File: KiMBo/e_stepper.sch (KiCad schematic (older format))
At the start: 24 parts, among them U18 TMC2130

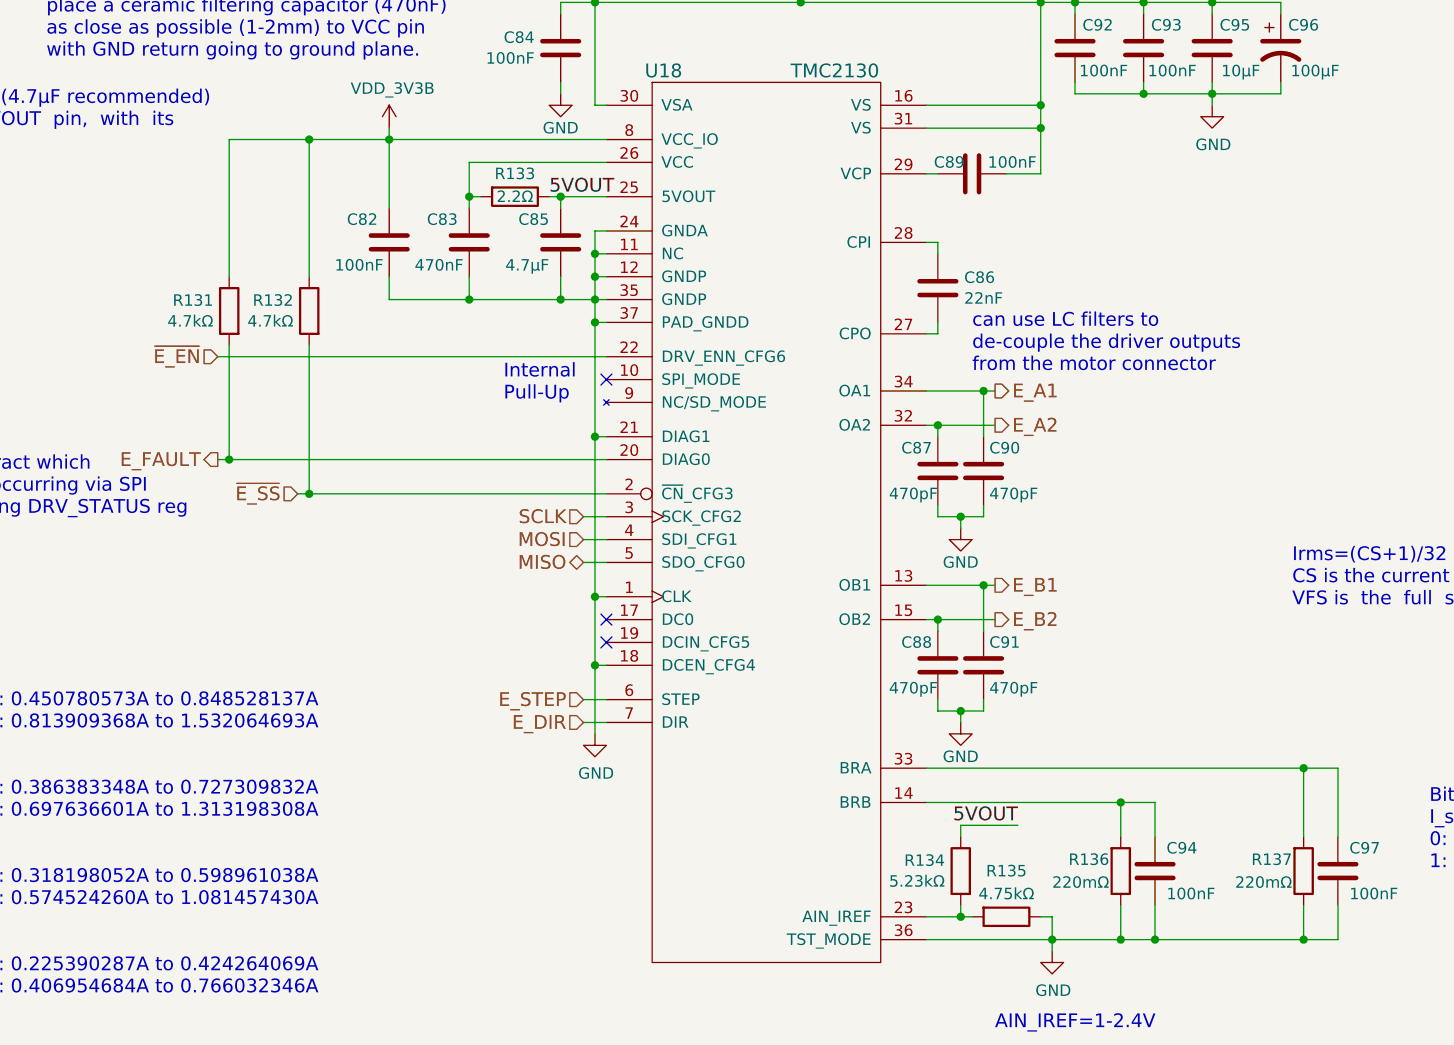
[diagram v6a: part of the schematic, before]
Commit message: Add more footprints and more associations, one association left!
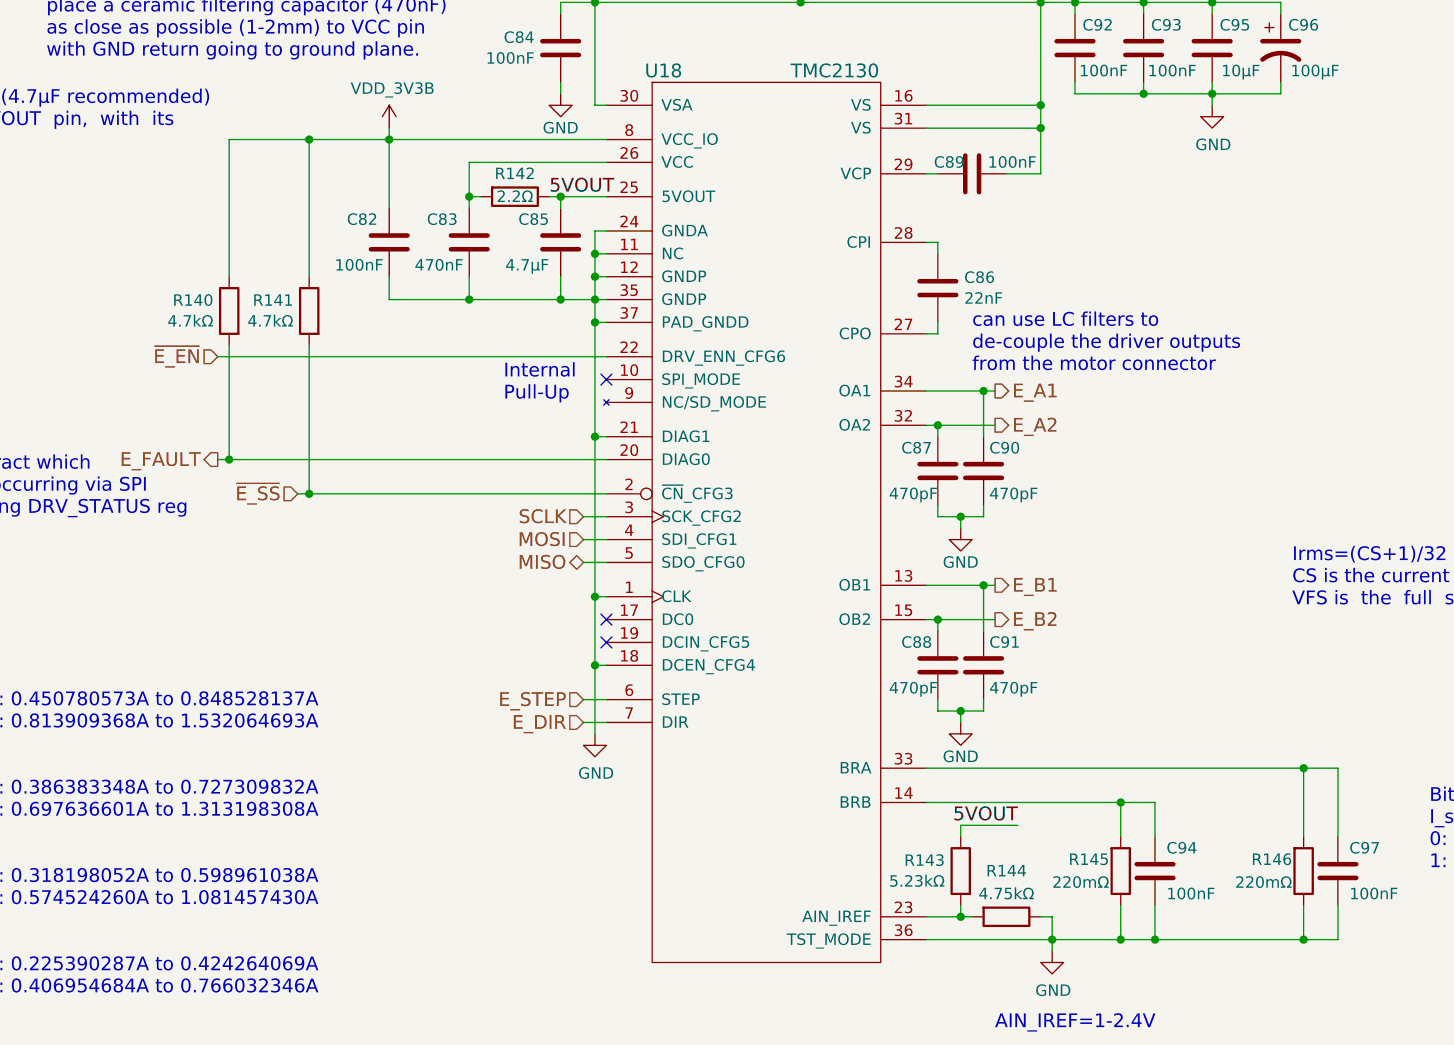
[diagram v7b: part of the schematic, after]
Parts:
- R144: renamed from R135; footprint Resistors_SMD:R_0603 -> Resistors_SMD:R_0805
- R146: renamed from R137; footprint Resistors_SMD:R_0805 -> Resistors_SMD:R_0603
- renumbered R131 to R140, R132 to R141, R133 to R142, R134 to R143, R136 to R145
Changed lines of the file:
@@
 $EndComp
 $Comp
-L GND #PWR0195
+L GND #PWR0197
 U 1 1 589BD203
 P 7300 4150
-F 0 "#PWR0195" H 7300 3900 50  0001 C CNN
+F 0 "#PWR0197" H 7300 3900 50  0001 C CNN
 F 1 "GND" H 7300 4000 50  0000 C CNN
 F 2 "" H 7300 4150 50  0000 C CNN
@@
 $EndComp
 $Comp
-L GND #PWR0196
+L GND #PWR0198
 U 1 1 589BE47E
 P 10150 4200
-F 0 "#PWR0196" H 10150 3950 50  0001 C CNN
+F 0 "#PWR0198" H 10150 3950 50  0001 C CNN
 F 1 "GND" H 10155 4027 50  0000 C CNN
 F 2 "" H 10150 4200 50  0000 C CNN
@@
 $EndComp
 $Comp
-L +24V #PWR0197
+L +24V #PWR0199
 U 1 1 5BA7E125
 P 8350 3700
-F 0 "#PWR0197" H 8350 3550 50  0001 C CNN
+F 0 "#PWR0199" H 8350 3550 50  0001 C CNN
 F 1 "+24V" H 8365 3873 50  0000 C CNN
 F 2 "" H 8350 3700 50  0000 C CNN
@@
 $EndComp
 $Comp
-L R R137
+L R R146
 U 1 1 589C1BED
 P 10550 7550
-F 0 "R137" H 10500 7500 50  0000 R CNN
+F 0 "R146" H 10500 7500 50  0000 R CNN
 F 1 "220mΩ" H 10500 7600 50  0000 R CNN
-F 2 "Resistors_SMD:R_0805" V 10480 7550 50  0001 C CNN
+F 2 "Resistors_SMD:R_0603" V 10480 7550 50  0001 C CNN
 F 3 "" H 10550 7550 50  0000 C CNN
 	1    10550 7550
@@
 $EndComp
 $Comp
-L R R136
+L R R145
 U 1 1 589C1CA7
 P 9750 7550
-F 0 "R136" H 9700 7500 50  0000 R CNN
+F 0 "R145" H 9700 7500 50  0000 R CNN
 F 1 "220mΩ" H 9700 7600 50  0000 R CNN
 F 2 "Resistors_SMD:R_0805" V 9680 7550 50  0001 C CNN
@@
 $EndComp
 $Comp
-L GND #PWR0198
+L GND #PWR0200
 U 1 1 5BA7E129
 P 9450 7900
-F 0 "#PWR0198" H 9450 7650 50  0001 C CNN
+F 0 "#PWR0200" H 9450 7650 50  0001 C CNN
 F 1 "GND" H 9455 7727 50  0000 C CNN
 F 2 "" H 9450 7900 50  0000 C CNN
@@
 NoConn ~ 7500 6450
 $Comp
-L R R133
+L R R142
 U 1 1 5BA7E12B
 P 7100 4600
-F 0 "R133" V 7000 4600 50  0000 C CNN
+F 0 "R142" V 7000 4600 50  0000 C CNN
 F 1 "2.2Ω" V 7100 4600 50  0000 C CNN
 F 2 "Resistors_SMD:R_0603" V 7030 4600 50  0001 C CNN
@@
 NoConn ~ 7500 6550
 $Comp
-L GND #PWR0199
+L GND #PWR0201
 U 1 1 589C97FF
 P 7450 6950
-F 0 "#PWR0199" H 7450 6700 50  0001 C CNN
+F 0 "#PWR0201" H 7450 6700 50  0001 C CNN
 F 1 "GND" H 7455 6777 50  0000 C CNN
 F 2 "" H 7450 6950 50  0000 C CNN
@@
 E_FAULT
 $Comp
-L R R131
+L R R140
 U 1 1 589D21BC
 P 5850 5100
-F 0 "R131" H 5919 5146 50  0000 L CNN
+F 0 "R140" H 5919 5146 50  0000 L CNN
 F 1 "4.7kΩ" H 5919 5055 50  0000 L CNN
 F 2 "Resistors_SMD:R_0603" V 5780 5100 50  0001 C CNN
@@
 5VOUT
 $Comp
-L R R134
+L R R143
 U 1 1 589E13FD
 P 9050 7550
-F 0 "R134" H 9119 7596 50  0000 L CNN
+F 0 "R143" H 9119 7596 50  0000 L CNN
 F 1 "5.23kΩ" H 9119 7505 50  0000 L CNN
 F 2 "Resistors_SMD:R_0603" V 8980 7550 50  0001 C CNN
@@
 5VOUT
 $Comp
-L R R135
+L R R144
 U 1 1 589E24D4
 P 9250 7750
-F 0 "R135" V 9050 7750 50  0000 C CNN
+F 0 "R144" V 9050 7750 50  0000 C CNN
 F 1 "4.75kΩ" V 9150 7750 50  0000 C CNN
-F 2 "Resistors_SMD:R_0603" V 9180 7750 50  0001 C CNN
+F 2 "Resistors_SMD:R_0805" V 9180 7750 50  0001 C CNN
 F 3 "" H 9250 7750 50  0000 C CNN
 	1    9250 7750
@@
 AIN_IREF=1-2.4V
 $Comp
-L R R132
+L R R141
 U 1 1 5BA7E132
 P 6200 5100
-F 0 "R132" H 6269 5146 50  0000 L CNN
+F 0 "R141" H 6269 5146 50  0000 L CNN
 F 1 "4.7kΩ" H 6269 5055 50  0000 L CNN
 F 2 "Resistors_SMD:R_0603" V 6130 5100 50  0001 C CNN
@@
 $EndComp
 $Comp
-L GND #PWR0200
+L GND #PWR0202
 U 1 1 58B19D33
 P 9050 6050
-F 0 "#PWR0200" H 9050 5800 50  0001 C CNN
+F 0 "#PWR0202" H 9050 5800 50  0001 C CNN
 F 1 "GND" H 9050 5900 50  0000 C CNN
 F 2 "" H 9050 6050 50  0000 C CNN
@@
 $EndComp
 $Comp
-L GND #PWR0201
+L GND #PWR0203
 U 1 1 58B1C704
 P 9050 6900
-F 0 "#PWR0201" H 9050 6650 50  0001 C CNN
+F 0 "#PWR0203" H 9050 6650 50  0001 C CNN
 F 1 "GND" H 9050 6750 50  0000 C CNN
 F 2 "" H 9050 6900 50  0000 C CNN
@@
 Can extract which\nfault is occurring via SPI\nby reading DRV_STATUS reg
 $Comp
-L VDD_3V3B #PWR0202
+L VDD_3V3B #PWR0204
 U 1 1 5A2FD350
 P 6550 4300
-F 0 "#PWR0202" H 6550 4150 50  0001 C CNN
+F 0 "#PWR0204" H 6550 4150 50  0001 C CNN
 F 1 "VDD_3V3B" H 6565 4473 50  0000 C CNN
 F 2 "" H 6550 4300 50  0000 C CNN
